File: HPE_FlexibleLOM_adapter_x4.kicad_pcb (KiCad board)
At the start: 4 copper layers, 79.2 x 21.7 mm, 9 parts, among them J1 Connector_PCIe_x8, J2 HPE_FlexibleLOM_x8

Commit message: RevB
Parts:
- removed JP1, JP2: Jumper_NC_Small, Jumper:SolderJumper-2_P1.3mm_Bridged_Pad1.0x1.5mm
- removed JP3: Jumper_3_Bridged12, Jumper:SolderJumper-3_P1.3mm_Bridged12_Pad1.0x1.5mm
- removed R1: 100kR, Resistor_SMD:R_0402_1005Metric
- moved R2 2.25 mm to (114.5, 109.2), turned to 180 degrees
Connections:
- J2 pad A1: Net-(J2-PadA1) -> +3V3
- J2 pad A14: Net-(J2-PadA14) -> /~PERST
- J2 pad B10: Net-(J2-PadB10) -> +3V3
- R2 pad 1: Net-(J2-PadA14) -> /~PERST
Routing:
- net +3V3: track 33.2 -> 57.8 mm
- net Net-(J2-PadA1): track 16.9 -> 0.00 mm
- net Net-(J2-PadA14): track 11.2 -> 0.00 mm
- net Net-(J2-PadB10): track 9.98 -> 0.00 mm
- net Net-(J2-PadB1): track 4.83 -> 0.00 mm
- net /PRSNT_x8: track 77.2 -> 75.4 mm
- net +12V: track 1.65 -> 0.00 mm
- net /~PERST: track 29.0 -> 28.5 mm
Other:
- board text added: "Rev B 2021"
- board text removed: "3v3 aux"
- board text removed: "Rev A 2020"
- board text removed: "~PERST"

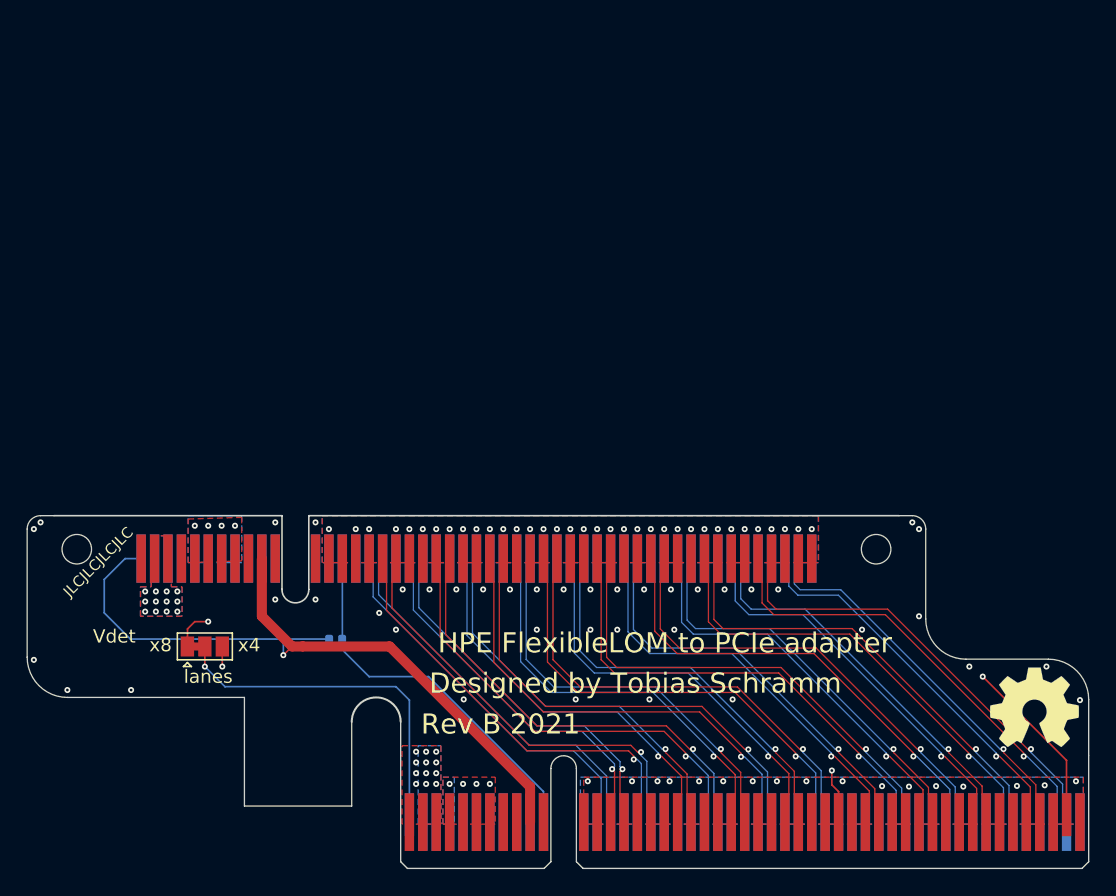
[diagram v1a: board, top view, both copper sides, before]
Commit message: Panelize RevB
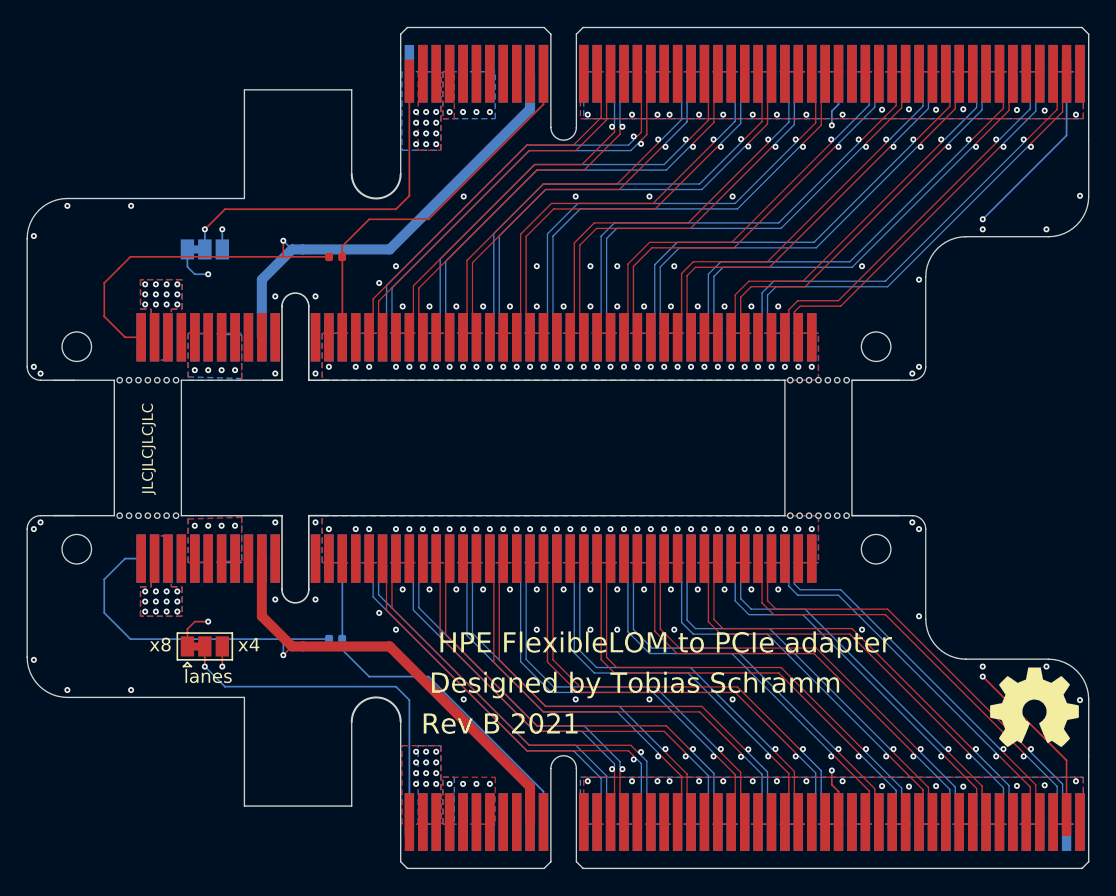
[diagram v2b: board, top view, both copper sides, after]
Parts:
- added H1: MountingHole, Symbol:OSHW-Symbol_6.7x6mm_SilkScreen, B.Cu at (166.6, 75.6)
- added J1: Connector_PCIe_x8, Connector_PCBEdge:BUS_PCIexpress_x8, B.Cu at (120.0, 67.0)
- added J2: HPE_FlexibleLOM_x8, Connector_PCIe:UMAX_3126-10102T_PCIe_x8_edge_launch, B.Cu at (100.0, 86.7)
- added JP4: Jumper_3_Bridged12, Jumper:SolderJumper-3_P1.3mm_Bridged12_Pad1.0x1.5mm, B.Cu at (104.8, 80.2)
- added R2: 100kR, Resistor_SMD:R_0402_1005Metric, F.Cu at (114.5, 80.7)
- added REF**: Perforation_0.4mm, Perforation:Perforation_0.4mm, B.Cu at (98.4, 89.9)
- added REF**: Perforation_0.4mm, Perforation:Perforation_0.4mm, B.Cu at (151.2, 89.9)
- added REF**: Perforation_0.4mm, Perforation:Perforation_0.4mm, B.Cu at (102.6, 89.9)
- added REF**: Perforation_0.4mm, Perforation:Perforation_0.4mm, B.Cu at (101.2, 89.9)
- added REF**: Perforation_0.4mm, Perforation:Perforation_0.4mm, B.Cu at (152.6, 89.9)
- added REF**: Perforation_0.4mm, Perforation:Perforation_0.4mm, B.Cu at (151.9, 89.9)
- added REF**: Perforation_0.4mm, Perforation:Perforation_0.4mm, F.Cu at (148.4, 100.0)
- added REF**: Perforation_0.4mm, Perforation:Perforation_0.4mm, F.Cu at (149.1, 100.0)
- added REF**: Perforation_0.4mm, Perforation:Perforation_0.4mm, F.Cu at (150.5, 100.0)
- added REF**: Perforation_0.4mm, Perforation:Perforation_0.4mm, F.Cu at (149.8, 100.0)
- added REF**: Perforation_0.4mm, Perforation:Perforation_0.4mm, F.Cu at (151.9, 100.0)
- added REF**: Perforation_0.4mm, Perforation:Perforation_0.4mm, B.Cu at (99.1, 89.9)
- added REF**: Perforation_0.4mm, Perforation:Perforation_0.4mm, F.Cu at (152.6, 100.0)
- added REF**: Perforation_0.4mm, Perforation:Perforation_0.4mm, F.Cu at (151.2, 100.0)
- added REF**: Perforation_0.4mm, Perforation:Perforation_0.4mm, F.Cu at (102.6, 100.0)
- added REF**: Perforation_0.4mm, Perforation:Perforation_0.4mm, F.Cu at (101.9, 100.0)
- added REF**: Perforation_0.4mm, Perforation:Perforation_0.4mm, F.Cu at (101.2, 100.0)
- added REF**: Perforation_0.4mm, Perforation:Perforation_0.4mm, F.Cu at (100.5, 100.0)
- added REF**: Perforation_0.4mm, Perforation:Perforation_0.4mm, F.Cu at (99.8, 100.0)
- added REF**: Perforation_0.4mm, Perforation:Perforation_0.4mm, F.Cu at (99.1, 100.0)
- added REF**: Perforation_0.4mm, Perforation:Perforation_0.4mm, F.Cu at (98.4, 100.0)
- added REF**: Perforation_0.4mm, Perforation:Perforation_0.4mm, B.Cu at (150.5, 89.9)
- added REF**: Perforation_0.4mm, Perforation:Perforation_0.4mm, B.Cu at (149.8, 89.9)
- added REF**: Perforation_0.4mm, Perforation:Perforation_0.4mm, B.Cu at (149.1, 89.9)
- added REF**: Perforation_0.4mm, Perforation:Perforation_0.4mm, B.Cu at (100.5, 89.9)
- added REF**: Perforation_0.4mm, Perforation:Perforation_0.4mm, B.Cu at (148.4, 89.9)
- added REF**: Perforation_0.4mm, Perforation:Perforation_0.4mm, B.Cu at (99.8, 89.9)
- added REF**: Perforation_0.4mm, Perforation:Perforation_0.4mm, B.Cu at (101.9, 89.9)
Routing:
- net (no net): track 0.00 -> 1334.6 mm, vias 0 -> 163
- added copper zone on B.Cu, net (none)
- added copper zone on F.Cu, net (none)
- added copper zone on GND1, net (none)
- added copper zone on GND2, net (none)
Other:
- board size 79.2 x 21.7 mm -> 79.2 x 53.4 mm
- board text removed: "Vdet"

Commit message: Update to experimental RevC
This recision connects some software defined pins to +3v3, some
more pins of unknown function and parts of the NC-SI interface
to GND. At least the latter should not be required to make any
FlexibleLOM card work. The impact of the former two needs to be
determined empirically.
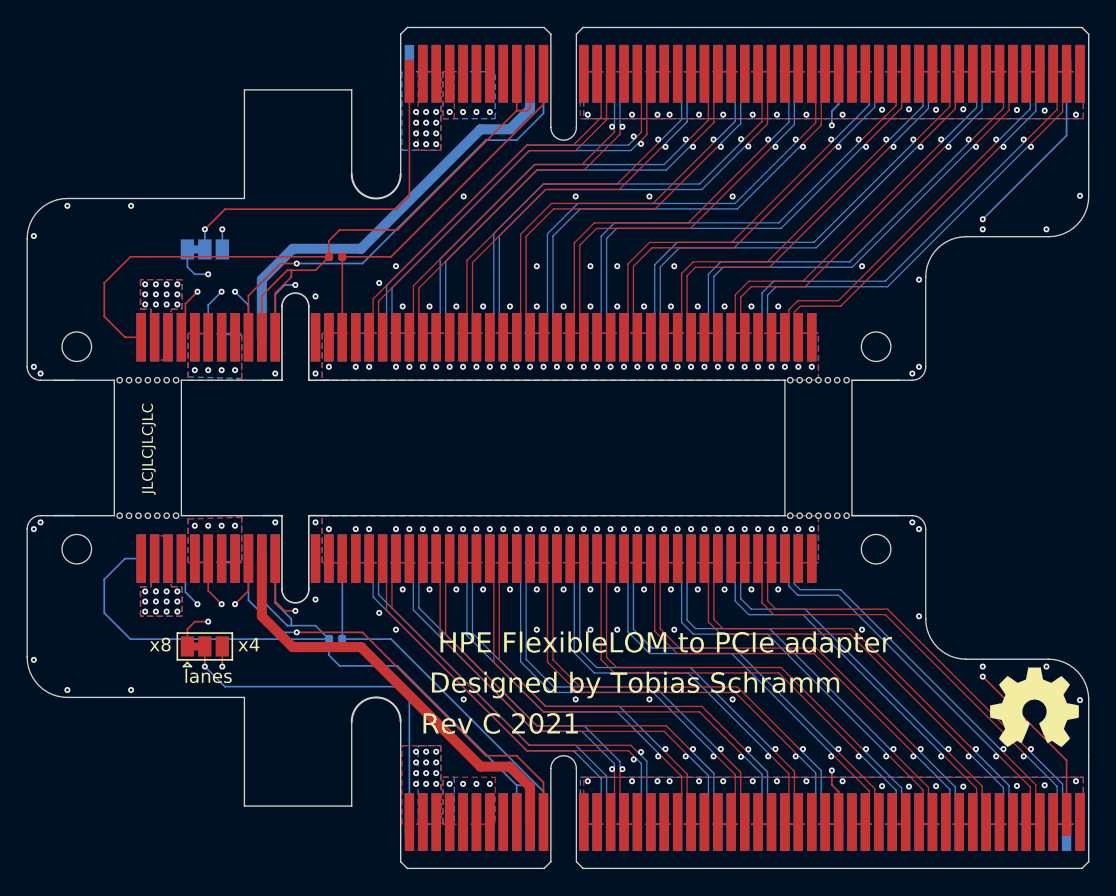
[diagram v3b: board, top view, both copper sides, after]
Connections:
- J1 pad A10: Net-(J1-PadA10) -> +3V3
- J1 pad A9: Net-(J1-PadA9) -> +3V3
- J1 pad B10: +3V3 -> /3v3_aux
- J1 pad B11: Net-(J1-PadB11) -> /~WAKE
- J2 pad A10: Net-(J2-PadA10) -> +3V3
- J2 pad A11: Net-(J2-PadA11) -> +3V3
- J2 pad A4: Net-(J2-PadA4) -> GND
- J2 pad A6: Net-(J2-PadA6) -> GND
- J2 pad A7: Net-(J2-PadA7) -> GND
- J2 pad A9: Net-(J2-PadA9) -> /~WAKE
- J2 pad B10: +3V3 -> /3v3_aux
- J2 pad B11: Net-(J2-PadB11) -> GND
- J2 pad B9: Net-(J2-PadB9) -> GND
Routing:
- net (no net): track 1334.6 -> 1422.4 mm, vias 163 -> 166
- net /~WAKE: track 0.00 -> 33.7 mm, vias 0 -> 1
- net /3v3_aux: track 0.00 -> 32.1 mm
- net GND: track 0.00 -> 16.5 mm, vias 101 -> 104
- net +3V3: track 57.8 -> 63.8 mm, vias 1 -> 0
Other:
- board text added: "Rev C 2021"
- board text removed: "Rev B 2021"
